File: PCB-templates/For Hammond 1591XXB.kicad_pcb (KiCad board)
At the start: 2 copper layers, 90.5 x 56 mm, 0 parts

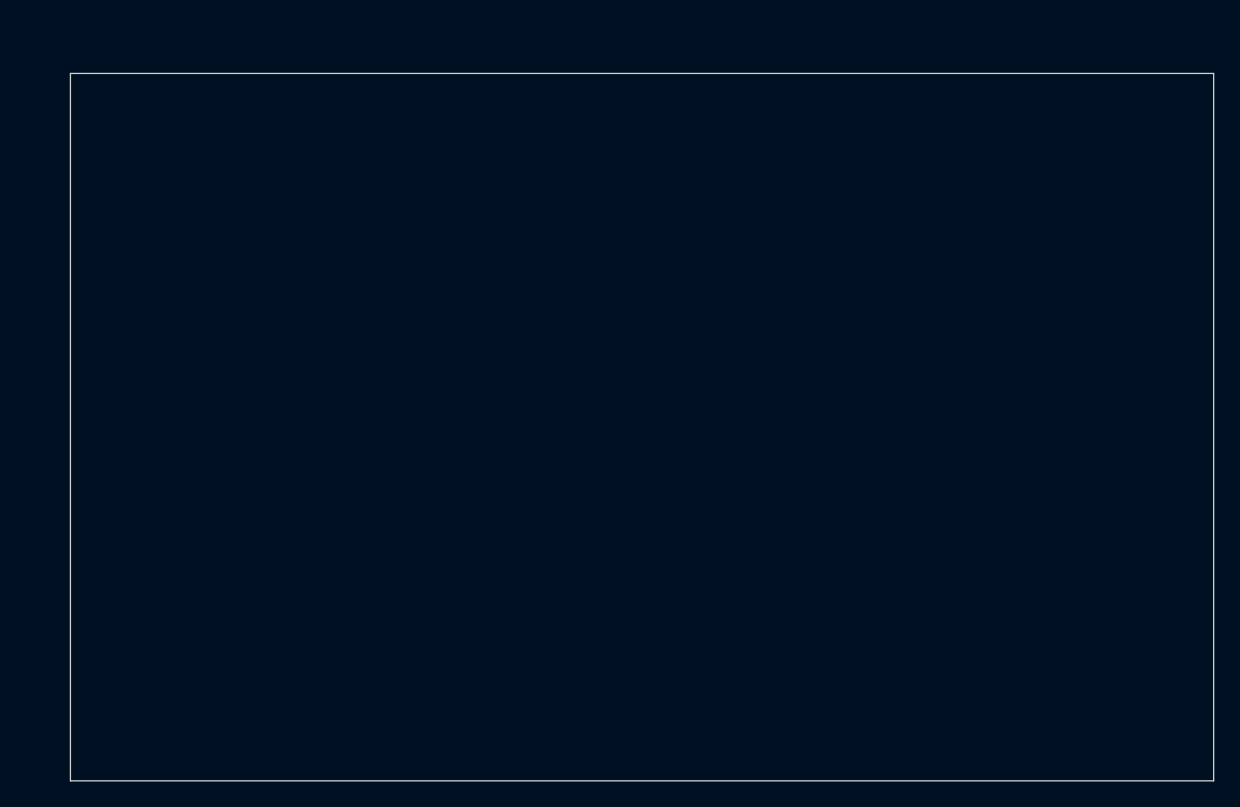
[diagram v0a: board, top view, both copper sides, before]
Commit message: Templates for Hammond 1591XXB redrawn, higher precision
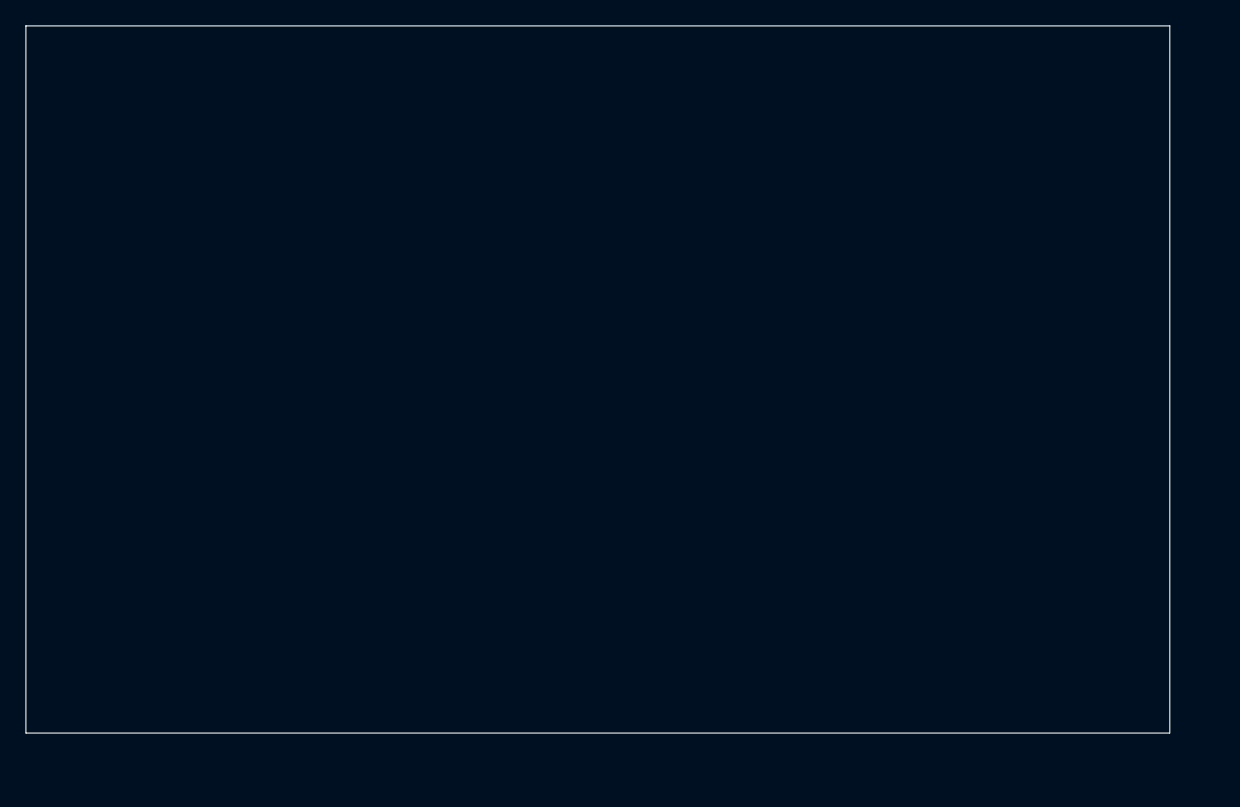
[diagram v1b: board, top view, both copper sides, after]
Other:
- board size 90.5 x 56 mm -> 90.6 x 56 mm
